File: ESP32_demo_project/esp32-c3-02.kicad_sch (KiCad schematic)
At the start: 15 parts, among them J3 GSD090012SEU, U3 ESP32-C3-WROOM-02-H4, U4 CP2102N-Axx-xQFN20, U5 USBLC6-2SC6, U6 W25Q32JVSSIQ

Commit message: main: update to project
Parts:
- added C12, C7: 10u, symbol Device:C_Polarized
- added C13, C14, C8: 0.1u, symbol Device:C
- added R15, R20: 50, symbol Device:R_US
- added R16, R22: 33.2, symbol Device:R_US
- added R17, R19, R21, R23: 10K, symbol Device:R_US
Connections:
- net +3.3V: now also J3.4 (VDD1), U3.1 (3V3), U6.8 (VCC), C12.1, C13.2, C14.2, C7.1, C8.2, R17.1, R19.2, R21.1, R23.1
- net GND: now also J3.1 (CD/DAT3), J3.3 (VSS1), J3.6 (VSS2), J3.8 (DAT1), J3.9 (DAT2), J3.G1 (SHIELD_GND), J3.G2 (SHIELD_GND), J3.G3 (SHIELD_GND), J3.G4 (SHIELD_GND), U3.18 (IO0), U3.19 (GND), U3.20 (GND), U3.21 (GND), U3.22 (GND), U3.23 (GND), U3.24 (GND), U3.25 (GND), U3.26 (GND), U3.27 (GND), U3.28 (GND), U3.29 (GND), U3.30 (GND), U3.31 (GND), U3.32 (GND), U3.33 (GND), U3.34 (GND), U3.35 (GND), U3.36 (GND), U3.37 (GND), U3.38 (GND), U3.39 (GND), U3.9 (GND), U6.1 (~{CS}), U6.4 (GND), C12.2, C13.1, C14.1, C7.2, C8.1, R19.1, R21.2
- net RX_TX: now also U3.12 (TXD)
- net TX_RX: now also U3.11 (RXD)
- net MOSI_DI: now reaches J3.2 (CMD)
- net MOSI_DI: now also U6.5 (DI(IO0)), R15.2
- net SCLK: now reaches J3.5 (CLK)
- net SCLK: now also U6.6 (CLK), R20.1
- net at J3.7 (DAT0): now also R16.1
- net at U6.2 (DO(IO1)): now also R22.2
- net at U6.3 (~{WP}(IO2)): now also R17.2
- net at U6.7 (~{HOLD}/~{RESET}(IO3)): now also R23.2
- net CS: now reaches U3.10 (IO10)
- net GPIO18: now reaches U3.13 (IO18)
- net GPIO19: now reaches U3.14 (IO19)
- net SCL: now reaches U3.15 (IO3)
- net MISO_DO: now reaches U3.16 (IO2)
- net MISO_DO: now also R16.2, R22.1
- net PHOTO_C: now reaches U3.17 (IO1)
- net EN: now reaches U3.2 (EN)
- net SDA: now reaches U3.3 (IO4)
- net MIC_OUT: now reaches U3.4 (IO5)
- net at U3.5 (IO6): now also R20.2
- net at U3.6 (IO7): now also R15.1
- net GPIO8: now reaches U3.7 (IO8)
- net BOOT: now reaches U3.8 (IO9)
- no-connect marks 5 -> 7
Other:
- note added: "ESP32-C3-02"
- note added: "Flash Memory"
- note added: "SD card module"
- moved on the sheet: J3, U3, U6

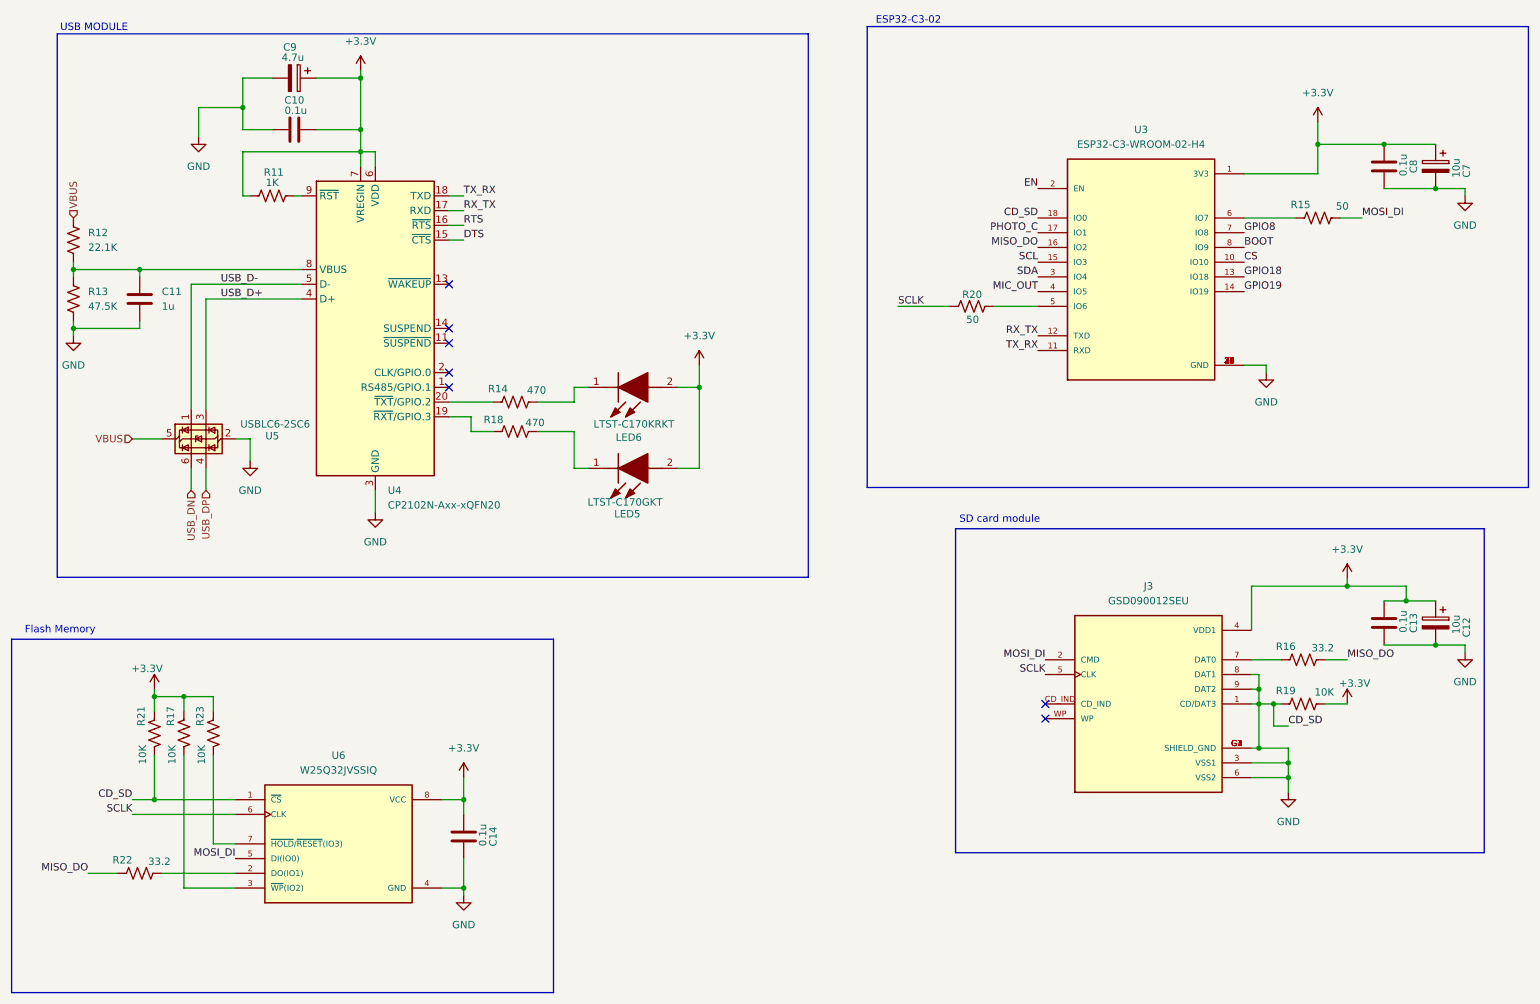
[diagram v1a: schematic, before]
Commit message: main: closed out schematics
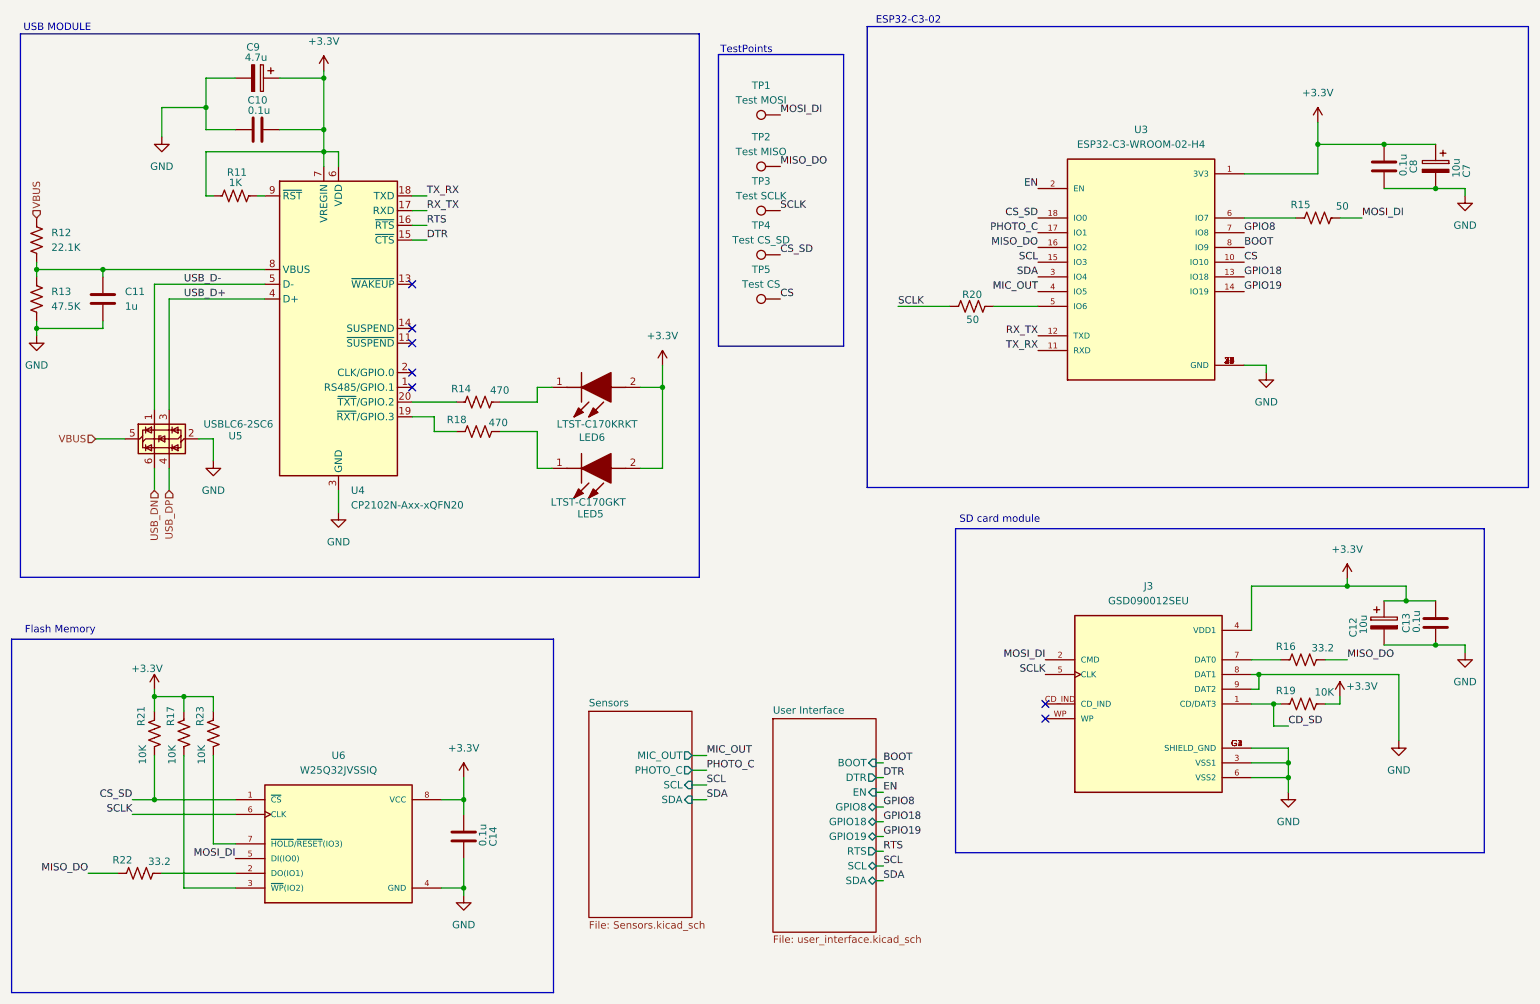
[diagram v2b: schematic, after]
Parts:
- added TP1: Test MOSI, TestPoint:TestPoint_Pad_D1.0mm, symbol Connector:TestPoint
- added TP2: Test MISO, TestPoint:TestPoint_Pad_D1.0mm, symbol Connector:TestPoint
- added TP3: Test SCLK, TestPoint:TestPoint_Pad_D1.0mm, symbol Connector:TestPoint
- added TP4: Test CS_SD, TestPoint:TestPoint_Pad_D1.0mm, symbol Connector:TestPoint
- added TP5: Test CS, TestPoint:TestPoint_Pad_D1.0mm, symbol Connector:TestPoint
- C10, C11, C13, C14, C8: footprint (none) -> Capacitor_SMD:C_0805_2012Metric
- C12, C7, C9: footprint (none) -> ESP32_project_Footprints:T491A
- LED5, LED6: footprint LEDC2012X120N -> ESP32_project_Footprints:LEDC2012X120N
- R11, R12, R13, R14, R15, R16, R17, R18, R19, R20, R21, R22, R23: footprint (none) -> Resistor_SMD:R_0805_2012Metric
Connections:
- net CS: now also TP5.1
- net GND: no longer J3.1 (CD/DAT3), R19.1, R21.2, U3.18 (IO0), U6.1 (~{CS})
- net MISO_DO: now also TP2.1
- net MOSI_DI: now also TP1.1
- net SCLK: now also TP3.1
- net DTS renamed DTR
- new net CD_SD: J3.1 (CD/DAT3), R19.1
- new net CS_SD: R21.2, TP4.1, U3.18 (IO0), U6.1 (~{CS})
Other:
- added sheet Sensors (Sensors.kicad_sch)
- added sheet User Interface (user_interface.kicad_sch)
- note added: "TestPoints"
- company: (none) -> Heratek
- title: (none) -> ESP32, C3, USB, and flash memory
- moved on the sheet: C10, C11, C12, C13, C9, LED5, LED6, R11, R12, R13, R14, R18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

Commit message: main: updating layout
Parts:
- J3: footprint GSD090012SEU:AMPHENOL_GSD090012SEU -> ESP32_project_Footprints:AMPHENOL_GSD090012SEU
- U3: footprint ESP32-C3-WROOM-02-H4:MODULE_ESP32-C3-WROOM-02-H4 -> ESP32_project_Footprints:MODULE_ESP32-C3-WROOM-02-H4
- U4: footprint Package_DFN_QFN:SiliconLabs_QFN-20-1EP_3x3mm_P0.5mm -> Package_DFN_QFN:SiliconLabs_QFN-20-1EP_3x3mm_P0.5mm_EP1.8x1.8mm
- U6: footprint W25Q32JVSSIQ:SOIC127P790X216-8N -> ESP32_project_Footprints:SOIC127P790X216-8N
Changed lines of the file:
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@@
 			)
 		)
-		(property "Footprint" "GSD090012SEU:AMPHENOL_GSD090012SEU"
+		(property "Footprint" "ESP32_project_Footprints:AMPHENOL_GSD090012SEU"
 			(at 210.82 135.89 0)
 			(effects
@@
 			)
 		)
-		(property "Footprint" "W25Q32JVSSIQ:SOIC127P790X216-8N"
+		(property "Footprint" "ESP32_project_Footprints:SOIC127P790X216-8N"
 			(at 71.12 160.02 0)
 			(effects
@@
 			)
 		)
-		(property "Footprint" "ESP32-C3-WROOM-02-H4:MODULE_ESP32-C3-WROOM-02-H4"
+		(property "Footprint" "ESP32_project_Footprints:MODULE_ESP32-C3-WROOM-02-H4"
 			(at 209.55 62.23 0)
 			(effects
@@
 			)
 		)
-		(property "Footprint" "Package_DFN_QFN:SiliconLabs_QFN-20-1EP_3x3mm_P0.5mm"
+		(property "Footprint" "Package_DFN_QFN:SiliconLabs_QFN-20-1EP_3x3mm_P0.5mm_EP1.8x1.8mm"
 			(at 102.87 97.79 0)
 			(effects
